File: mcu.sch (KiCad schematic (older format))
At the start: 28 parts, among them SW1 PTS645VL39-2, U4 CAT24C32, U5 STM32H743VI, X1 ECS-TXO-3225-200-TR

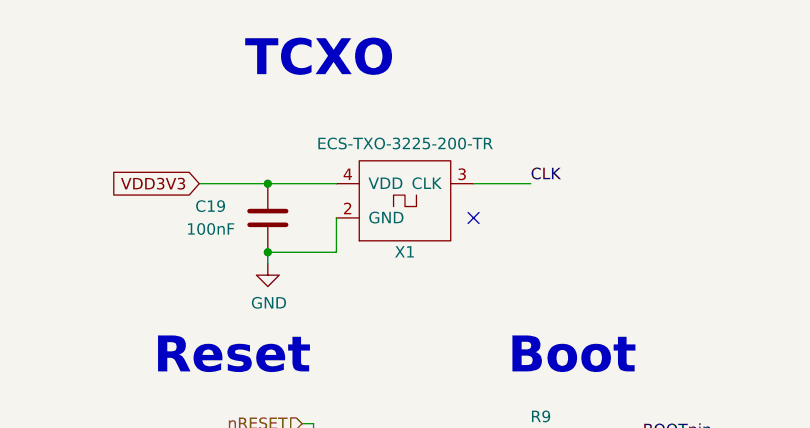
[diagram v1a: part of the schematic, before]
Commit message: Fixed wrong partnumber for TXCO
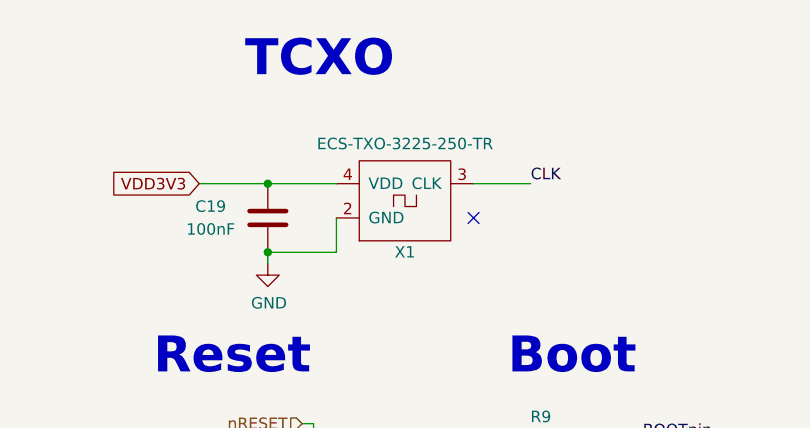
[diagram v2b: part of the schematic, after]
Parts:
- X1: value ECS-TXO-3225-200-TR -> ECS-TXO-3225-250-TR
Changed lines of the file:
@@
 P 2300 1350
 F 0 "X1" H 2300 1050 50  0000 C CNN
-F 1 "ECS-TXO-3225-200-TR" H 2300 1524 50  0000 C CNN
+F 1 "ECS-TXO-3225-250-TR" H 2300 1524 50  0000 C CNN
 F 2 "heteromycin:ECS-TXO-3225" H 2300 1350 157 0001 C CNN
 F 3 "https://www.ecsxtal.com/store/pdf/ECS-TXO-3225.pdf" H 2300 1350 157 0001 C CNN

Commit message: Added manufacturer number to schematic
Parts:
- C16, C17, C18, C19, C22, C23, C24, C25, C26, C27, C29: manf# (none) -> C0603C104M5RACTU
- C20, C21: manf# (none) -> 885012106022
- C28, C30: manf# (none) -> CGB3B1X5R1C225M055AC
- D6: manf# (none) -> LTST-C194KSKT
- FB2, FB3: manf# (none) -> MPZ1608S221A
- R10: manf# (none) -> CRCW0603100KFKEAC
- R11: manf# (none) -> RC0603JR-7W1KL
- R12, R13: manf# (none) -> AC0603JR-074K7L
- R9: manf# (none) -> AC0603FR-0710KL
- SW1: manf# (none) -> PTS645VL392LFS
- U4: manf# (none) -> CAT24C32WI-GT3
- U5: manf# (none) -> STM32H743VI
- X1: manf# (none) -> ECS-TXO-3225-250-TR
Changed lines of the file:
@@
 F 2 "Capacitor_SMD:C_0603_1608Metric" H 1838 6500 50  0001 C CNN
 F 3 "~" H 1800 6650 50  0001 C CNN
+F 4 "885012106022" H 0   0   50  0001 C CNN "manf#"
 	1    1800 6650
 	1    0    0    -1
@@
 F 2 "Capacitor_SMD:C_0603_1608Metric" H 2238 6500 50  0001 C CNN
 F 3 "~" H 2200 6650 50  0001 C CNN
+F 4 "C0603C104M5RACTU" H 0   0   50  0001 C CNN "manf#"
 	1    2200 6650
 	1    0    0    -1
@@
 F 2 "Capacitor_SMD:C_0603_1608Metric" H 1838 6100 50  0001 C CNN
 F 3 "~" H 1800 6250 50  0001 C CNN
+F 4 "885012106022" H 0   0   50  0001 C CNN "manf#"
 	1    1800 6250
 	1    0    0    -1
@@
 F 2 "Capacitor_SMD:C_0603_1608Metric" H 2238 6100 50  0001 C CNN
 F 3 "~" H 2200 6250 50  0001 C CNN
+F 4 "C0603C104M5RACTU" H 0   0   50  0001 C CNN "manf#"
 	1    2200 6250
 	1    0    0    -1
@@
 F 2 "Capacitor_SMD:C_0603_1608Metric" H 1188 7150 50  0001 C CNN
 F 3 "~" H 1150 7300 50  0001 C CNN
+F 4 "C0603C104M5RACTU" H 0   0   50  0001 C CNN "manf#"
 	1    1150 7300
 	1    0    0    -1
@@
 F 2 "Capacitor_SMD:C_0603_1608Metric" H 1638 7150 50  0001 C CNN
 F 3 "~" H 1600 7300 50  0001 C CNN
+F 4 "C0603C104M5RACTU" H 0   0   50  0001 C CNN "manf#"
 	1    1600 7300
 	1    0    0    -1
@@
 F 2 "Capacitor_SMD:C_0603_1608Metric" H 2088 7150 50  0001 C CNN
 F 3 "~" H 2050 7300 50  0001 C CNN
+F 4 "C0603C104M5RACTU" H 0   0   50  0001 C CNN "manf#"
 	1    2050 7300
 	1    0    0    -1
@@
 F 2 "Capacitor_SMD:C_0603_1608Metric" H 2538 7150 50  0001 C CNN
 F 3 "~" H 2500 7300 50  0001 C CNN
+F 4 "C0603C104M5RACTU" H 0   0   50  0001 C CNN "manf#"
 	1    2500 7300
 	1    0    0    -1
@@
 F 2 "Capacitor_SMD:C_0603_1608Metric" H 2988 7150 50  0001 C CNN
 F 3 "~" H 2950 7300 50  0001 C CNN
+F 4 "C0603C104M5RACTU" H 0   0   50  0001 C CNN "manf#"
 	1    2950 7300
 	1    0    0    -1
@@
 F 2 "Capacitor_SMD:C_0603_1608Metric" H 3288 6300 50  0001 C CNN
 F 3 "~" H 3250 6450 50  0001 C CNN
+F 4 "CGB3B1X5R1C225M055AC" H 0   0   50  0001 C CNN "manf#"
 	1    3250 6450
 	-1   0    0    1
@@
 F 2 "Capacitor_SMD:C_0603_1608Metric" H 3688 6300 50  0001 C CNN
 F 3 "~" H 3650 6450 50  0001 C CNN
+F 4 "CGB3B1X5R1C225M055AC" H 0   0   50  0001 C CNN "manf#"
 	1    3650 6450
 	-1   0    0    1
@@
 F 2 "Button_Switch_THT:SW_Tactile_SPST_Angled_PTS645Vx39-2LFS" H 1550 3050 50  0001 C CNN
 F 3 "https://www.mouser.de/datasheet/2/60/-1131575.pdf" H 1550 3050 50  0001 C CNN
+F 4 "PTS645VL392LFS" H 0   0   50  0001 C CNN "manf#"
 	1    1550 2850
 	1    0    0    -1
@@
 F 2 "Capacitor_SMD:C_0603_1608Metric" H 1588 3050 50  0001 C CNN
 F 3 "~" H 1550 3200 50  0001 C CNN
+F 4 "C0603C104M5RACTU" H 0   0   50  0001 C CNN "manf#"
 	1    1550 3200
 	0    -1   -1   0
@@
 F 2 "Resistor_SMD:R_0603_1608Metric" V 1180 6400 50  0001 C CNN
 F 3 "https://www.mouser.de/datasheet/2/400/eads_commercial_power_mpz1608_en-923650.pdf" H 1250 6400 50  0001 C CNN
+F 4 "MPZ1608S221A" H 0   0   50  0001 C CNN "manf#"
 	1    1250 6400
 	0    1    1    0
@@
 F 2 "Resistor_SMD:R_0603_1608Metric" V 1280 6500 50  0001 C CNN
 F 3 "https://www.mouser.de/datasheet/2/400/eads_commercial_power_mpz1608_en-923650.pdf" H 1350 6500 50  0001 C CNN
+F 4 "MPZ1608S221A" H 0   0   50  0001 C CNN "manf#"
 	1    1350 6500
 	0    1    1    0
@@
 F 2 "heteromycin:ECS-TXO-3225" H 2300 1350 157 0001 C CNN
 F 3 "https://www.ecsxtal.com/store/pdf/ECS-TXO-3225.pdf" H 2300 1350 157 0001 C CNN
+F 4 "ECS-TXO-3225-250-TR" H 0   0   50  0001 C CNN "manf#"
 	1    2300 1350
 	1    0    0    -1
@@
 F 2 "Capacitor_SMD:C_0603_1608Metric" H 1738 1350 50  0001 C CNN
 F 3 "~" H 1700 1500 50  0001 C CNN
+F 4 "C0603C104M5RACTU" H 0   0   50  0001 C CNN "manf#"
 	1    1700 1500
 	1    0    0    -1
@@
 F 2 "Package_SO:SOIC-8_3.9x4.9mm_P1.27mm" H 1900 4350 50  0001 C CNN
 F 3 "" H 1900 4350 50  0000 C CNN
+F 4 "CAT24C32WI-GT3" H 0   0   50  0001 C CNN "manf#"
 	1    1900 4350
 	1    0    0    -1
@@
 F 2 "Capacitor_SMD:C_0603_1608Metric" H 3438 7150 50  0001 C CNN
 F 3 "~" H 3400 7300 50  0001 C CNN
+F 4 "C0603C104M5RACTU" H 0   0   50  0001 C CNN "manf#"
 	1    3400 7300
 	1    0    0    -1
@@
 F 2 "Resistor_SMD:R_0603_1608Metric" V 9530 5950 50  0001 C CNN
 F 3 "~" H 9600 5950 50  0001 C CNN
+F 4 "AC0603JR-074K7L" H 0   0   50  0001 C CNN "manf#"
 	1    9600 5950
 	-1   0    0    1
@@
 F 2 "Resistor_SMD:R_0603_1608Metric" V 9830 5950 50  0001 C CNN
 F 3 "~" H 9900 5950 50  0001 C CNN
+F 4 "AC0603JR-074K7L" H 0   0   50  0001 C CNN "manf#"
 	1    9900 5950
 	-1   0    0    1
@@
 F 2 "Resistor_SMD:R_0603_1608Metric" V 5480 6250 50  0001 C CNN
 F 3 "~" H 5550 6250 50  0001 C CNN
+F 4 "RC0603JR-7W1KL" H 0   0   50  0001 C CNN "manf#"
 	1    5550 6250
 	1    0    0    -1
@@
 F 2 "LED_SMD:LED_0603_1608Metric" H 5550 6550 50  0001 C CNN
 F 3 "~" H 5550 6550 50  0001 C CNN
+F 4 "LTST-C194KSKT" H 0   0   50  0001 C CNN "manf#"
 	1    5550 6550
 	0    -1   -1   0
@@
 F 2 "Capacitor_SMD:C_0603_1608Metric" H 2588 3800 50  0001 C CNN
 F 3 "~" H 2550 3950 50  0001 C CNN
+F 4 "C0603C104M5RACTU" H 0   0   50  0001 C CNN "manf#"
 	1    2550 3950
 	1    0    0    -1
@@
 F 2 "heteromycin:TQFP-100_14x14mm_P0.5mm" H 6750 3000 50  0001 C CNN
 F 3 "https://www.st.com/en/microcontrollers/stm32h743vi.html" H 6750 3000 50  0001 C CNN
+F 4 "STM32H743VI" H 6750 3000 50  0001 C CNN "manf#"
 	1    6750 3000
 	1    0    0    -1
@@
 F 2 "Resistor_SMD:R_0603_1608Metric" V 2820 2470 50  0001 C CNN
 F 3 "~" H 2890 2470 50  0001 C CNN
+F 4 "AC0603FR-0710KL" H 0   0   50  0001 C CNN "manf#"
 	1    2890 2470
 	0    -1   -1   0
@@
 F 2 "Resistor_SMD:R_0603_1608Metric" V 3070 2620 50  0001 C CNN
 F 3 "~" H 3140 2620 50  0001 C CNN
+F 4 "CRCW0603100KFKEAC" H 0   0   50  0001 C CNN "manf#"
 	1    3140 2620
 	-1   0    0    1
